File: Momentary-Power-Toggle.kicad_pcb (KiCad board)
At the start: 2 copper layers, 14.5 x 13 mm, 14 parts, among them Q1 IRF7317PbF, SW1 ON / OFF Button

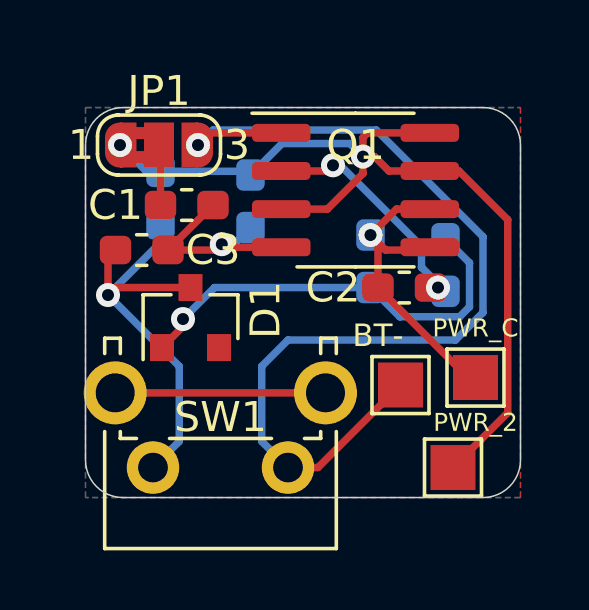
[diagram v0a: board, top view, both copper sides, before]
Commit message: Add files via upload
fixed schematic error
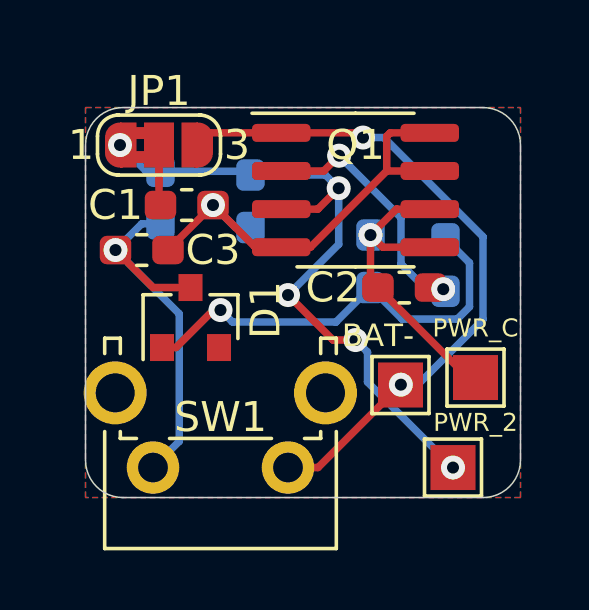
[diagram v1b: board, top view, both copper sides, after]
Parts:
- D1: value BAV99 -> MMBD7000LT1G
- renumbered BT- to BAT-
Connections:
- C1 pad 1: Net-(C1-Pad1) -> D1
- C3 pad 1: Net-(C1-Pad1) -> D1
- JP1 pad 1: D1 -> VCC
- PWR_2 pad 1: D1 -> VCC
- Q1 pad 3: D1 -> VCC
- Q1 pad 4: Net-(C1-Pad1) -> D1
- R1 pad 1: D1 -> VCC
- R2 pad 1: D1 -> VCC
- R2 pad 2: Net-(C1-Pad1) -> D1
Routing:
- net VCC: track 0.00 -> 22.8 mm, vias 0 -> 5
- net GND: track 40.4 -> 22.4 mm, vias 1 -> 2
- net D1: track 30.5 -> 15.2 mm, vias 2 -> 1
- net Net-(C1-Pad1): track 7.21 -> 0.00 mm, vias 1 -> 0
- net Net-(C3-Pad2): track 14.7 -> 13.4 mm
- net Net-(C2-Pad1): track 7.70 -> 8.46 mm

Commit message: updated design rules on PCB
oshpark preview exposed an error with my design rule settings
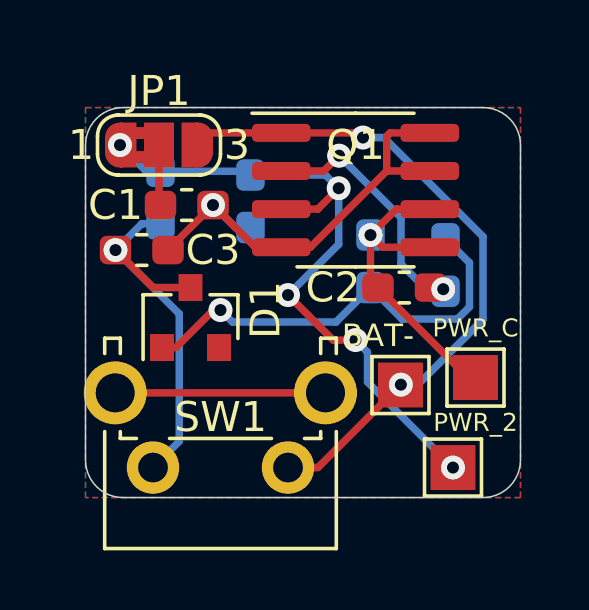
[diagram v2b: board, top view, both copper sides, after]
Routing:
- net GND: track 22.4 -> 29.4 mm
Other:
- rule solder_mask_min_width: 0.25 -> 0.1
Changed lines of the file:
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@@
     (thickness 1.6)
     (drawings 8)
-    (tracks 86)
+    (tracks 87)
     (zones 0)
     (modules 14)
@@
     (pad_drill 1.3)
     (pad_to_mask_clearance 0.051)
-    (solder_mask_min_width 0.25)
+    (solder_mask_min_width 0.1)
     (aux_axis_origin 0 0)
     (visible_elements 7FFFFFFF)
@@
   (via (at 92.76266 84.98734) (size 0.8) (drill 0.4) (layers F.Cu B.Cu) (net 1))
   (segment (start 95.50002 82.815665) (end 93.328345 84.98734) (width 0.25) (layer B.Cu) (net 1))
+  (segment (start 90.25 85.26) (end 83.24 85.26) (width 0.25) (layer F.Cu) (net 1))
   (segment (start 84.7 78.95) (end 84.75 79) (width 0.25) (layer F.Cu) (net 2))
   (segment (start 84.7 77) (end 84.7 78.95) (width 0.25) (layer F.Cu) (net 2))
@@
   (zone (net 1) (net_name GND) (layer F.Cu) (hatch edge 0.508)
     (connect_pads (clearance 0.508))
-    (min_thickness 0.254)
+    (min_thickness 0.1)
     (fill yes (arc_segments 32) (thermal_gap 0.508) (thermal_bridge_width 0.508))
     (polygon
@@
   (zone (net 1) (net_name GND) (layer B.Cu) (hatch edge 0.508)
     (connect_pads (clearance 0.508))
-    (min_thickness 0.254)
+    (min_thickness 0.1)
     (fill yes (arc_segments 32) (thermal_gap 0.508) (thermal_bridge_width 0.508))
     (polygon

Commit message: general cleanup
defuckulated the repository by removing obsolete board configs, updating schematic image, condensing readmes, etc
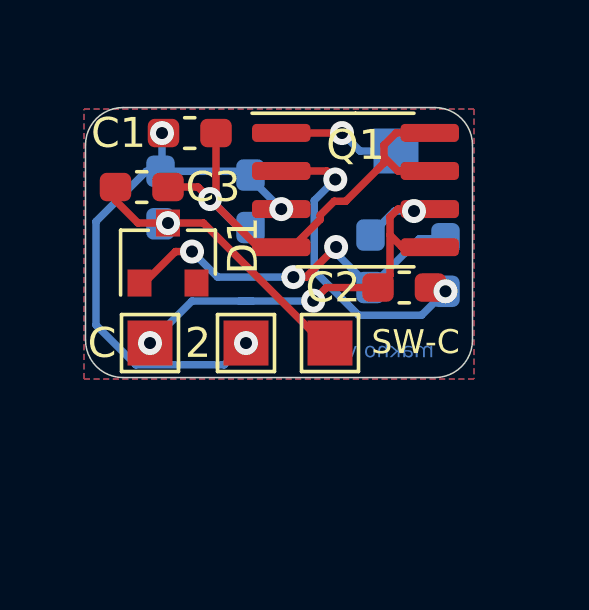
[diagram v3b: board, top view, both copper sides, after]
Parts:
- removed BAT-: BT-, TestPoint:TestPoint_Pad_1.5x1.5mm
- removed JP1: Power On Setting, Jumper:SolderJumper-3_P1.3mm_Bridged2Bar12_RoundedPad1.0x1.5mm_NumberLabels
- removed PWR_2: PWR_2, TestPoint:TestPoint_Pad_1.5x1.5mm
- removed PWR_C: PWR_C, TestPoint:TestPoint_Pad_1.5x1.5mm
- removed SW1: ON / OFF Button, Button_Switch_THT:SW_Tactile_SPST_Angled_PTS645Vx83-2LFS
- added 2: PWR_2, TestPoint:TestPoint_Pad_1.5x1.5mm, F.Cu at (87.6, 83.6)
- added C: PWR_C, TestPoint:TestPoint_Pad_1.5x1.5mm, F.Cu at (84.4, 83.6)
- added GND: GND, TestPoint:TestPoint_Pad_1.5x1.5mm, B.Cu at (92.6, 77.2)
- added SW-C: BTN, TestPoint:TestPoint_Pad_1.5x1.5mm, F.Cu at (90.4, 83.6)
- moved C1 2.40 mm to (85.7, 76.6)
- moved D1 2.28 mm to (85.0, 80.6)
- moved C3 2.10 mm to (84.1, 78.4)
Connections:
- C1 pad 2: Net-(C1-Pad2) -> VCC
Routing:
- net GND: track 29.4 -> 4.08 mm, vias 2 -> 1
- net Net-(C2-Pad2): track 10.8 -> 16.5 mm, vias 1 -> 3
- net VCC: track 22.8 -> 18.1 mm, vias 5 -> 3
- net Net-(C3-Pad2): track 13.4 -> 9.83 mm
- net Net-(C2-Pad1): track 8.46 -> 11.1 mm
- net D1: track 15.2 -> 17.7 mm
- net Net-(C1-Pad2): track 2.02 -> 0.00 mm
- net Net-(D1-Pad2): track 14.6 -> 12.8 mm, vias 1 -> 3
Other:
- board size 14.5 x 13 mm -> 12.9 x 9 mm
- board text added: "https://github.com /makhowastaken /Soft-Latching-Power-Button"
- board text added: "makho v2.1"

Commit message: update kicad files (ver 5 -> ver 6)
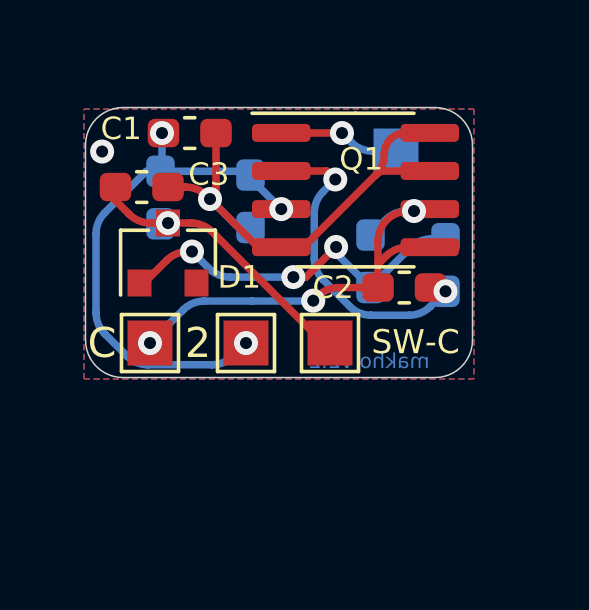
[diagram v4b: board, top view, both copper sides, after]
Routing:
- net Net-(C2-Pad2): track 16.5 -> 15.7 mm
- net GND: track 4.08 -> 4.03 mm, vias 1 -> 2
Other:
- net class Default removed
- board text added: "makho v2.2"
- board text removed: "makho v2.1"
